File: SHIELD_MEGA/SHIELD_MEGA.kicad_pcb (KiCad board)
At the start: 2 copper layers, 101.6 x 53.3 mm, 81 parts, among them J1 Conn_02x03_Odd_Even, J10 Conn_01x03_Female, J11 DF13-6P-1.25DSA, J12 Conn_01x04_Male, J13 Conn_01x04_Male, J14 Conn_02x03_Odd_Even, J15 Conn_01x04_Male, J16 Conn_01x03_Male, J17 Conn_01x03_Male, J18 Conn_01x03_Male, J19 Conn_01x03_Male, J2 Conn_02x03_Odd_Even, J20 Conn_01x03_Male, J21 Conn_01x03_Male, J22 Conn_01x03_Male, J23 Conn_01x03_Male, J24 Conn_01x03_Male, J25 Conn_01x03_Male, J26 Conn_01x03_Male, J27 Conn_01x03_Male, J28 Conn_01x03_Male, J29 Conn_01x03_Male, J3 Conn_02x03_Odd_Even, J30 Conn_01x03_Male, J31 Conn_01x03_Male, J32 Conn_01x03_Male, J33 Conn_01x03_Male, J34 Conn_01x03_Male, J35 Conn_01x03_Male, J36 Conn_01x03_Male, J37 Conn_01x03_Male, J38 Conn_01x03_Male, J39 Conn_01x03_Male, J40 Conn_01x03_Male, J41 Conn_01x03_Male, J42 Conn_01x03_Male, J43 Conn_01x03_Male, J44 Conn_01x03_Male, J45 Conn_01x03_Male, J46 Conn_01x03_Male, J47 Conn_01x03_Male, J48 Conn_01x03_Male, J49 Conn_01x03_Male, J5 Conn_01x02_Male, J50 Conn_01x03_Male, J51 Conn_01x03_Male, J52 Conn_01x03_Male, J53 Conn_01x03_Male, J54 Conn_01x03_Male, J55 Conn_01x03_Male, J56 Conn_01x03_Male, J57 Conn_01x03_Male, J58 Conn_01x03_Male, J59 Conn_01x03_Male, J6 Conn_01x07_Female, J60 Conn_01x03_Male, J61 Conn_01x03_Male, J62 Conn_01x03_Male, J63 Conn_01x03_Male, J64 Conn_01x03_Male, J65 Conn_01x03_Male, J66 Conn_01x03_Female, J67 Conn_01x03_Female, J68 Conn_01x03_Female, J69 Conn_01x03_Female, J7 Conn_01x03_Female, J70 Conn_01x03_Female, J71 Conn_01x03_Female, J72 Conn_01x03_Female, J73 Conn_01x06_Female, J8 Conn_01x03_Female, J9 Conn_01x03_Female, SW1 SW_MEC_5E

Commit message: Changes in PCB
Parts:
- removed J14: Conn_02x03_Odd_Even, Connector_PinSocket_2.54mm:PinSocket_2x03_P2.54mm_Vertical
- removed J59, J60, J61: Conn_01x03_Male, Connector_PinHeader_2.54mm:PinHeader_1x03_P2.54mm_Vertical
- removed L1, L2: Inductor_15uH_1.9A, Inductor_SMD:L_0805_2012Metric_Pad1.15x1.40mm_HandSolder
- added D1: LED_ARBG, LED_ARBG:LED_LL-R3528RGBC-008-B, F.Cu at (135.4, 97.9)
- added G***: LOGO, LOGO:LOGO_NOVO, F.Cu at (106.3, 78.0)
- added R2: 3k3, Resistor_SMD:R_0805_2012Metric_Pad1.20x1.40mm_HandSolder, F.Cu at (143.6, 98.8)
- added R3: 3k3, Resistor_SMD:R_0805_2012Metric_Pad1.20x1.40mm_HandSolder, F.Cu at (143.7, 96.3)
- added R4: 3k3, Resistor_SMD:R_0805_2012Metric_Pad1.20x1.40mm_HandSolder, F.Cu at (143.6, 93.9)
- moved J58 127.0 mm to (129.7, 85.1)
- moved J57 120.2 mm to (132.2, 85.1)
- moved J43 107.3 mm to (188.7, 93.5), turned to 270 degrees
- moved J51 101.5 mm to (147.4, 85.1)
- moved J48 90.3 mm to (155.1, 85.1)
- moved J34 86.2 mm to (188.7, 70.6), turned to 270 degrees
- moved J45 85.8 mm to (188.7, 98.6), turned to 270 degrees
- moved J42 85.5 mm to (188.7, 90.9), turned to 270 degrees
- moved J47 83.8 mm to (157.6, 85.1)
- moved J46 77.5 mm to (160.1, 85.1)
- moved J56 73.9 mm to (134.7, 85.1)
- moved J52 61.7 mm to (144.9, 85.1)
- moved J35 57.0 mm to (188.7, 73.2), turned to 270 degrees
- moved J44 56.9 mm to (188.7, 96.0), turned to 270 degrees
- moved J53 56.6 mm to (142.4, 85.1)
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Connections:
- J12 pad 4: /arduino_mega_2560/DGND -> GND
- J13 pad 4: /arduino_mega_2560/DGND -> GND
- J15 pad 4: /arduino_mega_2560/DGND -> GND
- J16 pad 3: /arduino_mega_2560/AGND -> GND
- J17 pad 3: /arduino_mega_2560/AGND -> GND
- J18 pad 3: /arduino_mega_2560/AGND -> GND
- J19 pad 3: /arduino_mega_2560/AGND -> GND
- J20 pad 3: /arduino_mega_2560/AGND -> GND
- J21 pad 3: /arduino_mega_2560/AGND -> GND
- J22 pad 3: /arduino_mega_2560/AGND -> GND
- J23 pad 3: /arduino_mega_2560/AGND -> GND
- J24 pad 3: /arduino_mega_2560/AGND -> GND
- J25 pad 3: /arduino_mega_2560/AGND -> GND
- J26 pad 3: /arduino_mega_2560/AGND -> GND
- J27 pad 3: /arduino_mega_2560/AGND -> GND
- J28 pad 3: /arduino_mega_2560/AGND -> GND
- J29 pad 3: /arduino_mega_2560/AGND -> GND
- J3 pad 5: /arduino_mega_2560/DGND -> GND
- J30 pad 3: /arduino_mega_2560/AGND -> GND
- J31 pad 3: /arduino_mega_2560/AGND -> GND
- J32 pad 3: /arduino_mega_2560/DGND -> GND
- J33 pad 3: /arduino_mega_2560/DGND -> GND
- J34 pad 3: /arduino_mega_2560/DGND -> GND
- J35 pad 3: /arduino_mega_2560/DGND -> GND
- J36 pad 3: /arduino_mega_2560/DGND -> GND
- J37 pad 3: /arduino_mega_2560/DGND -> GND
- J38 pad 3: /arduino_mega_2560/DGND -> GND
- J39 pad 3: /arduino_mega_2560/DGND -> GND
- J40 pad 3: /arduino_mega_2560/DGND -> GND
- J41 pad 3: /arduino_mega_2560/DGND -> GND
- J42 pad 3: /arduino_mega_2560/DGND -> GND
- J43 pad 3: /arduino_mega_2560/DGND -> GND
- J44 pad 3: /arduino_mega_2560/DGND -> GND
- J45 pad 3: /arduino_mega_2560/DGND -> GND
- J46 pad 3: /arduino_mega_2560/DGND -> GND
- J47 pad 3: /arduino_mega_2560/DGND -> GND
- J48 pad 3: /arduino_mega_2560/DGND -> GND
- J49 pad 3: /arduino_mega_2560/DGND -> GND
- J50 pad 3: /arduino_mega_2560/DGND -> GND
- J51 pad 3: /arduino_mega_2560/DGND -> GND
- J52 pad 3: /arduino_mega_2560/DGND -> GND
- J53 pad 3: /arduino_mega_2560/DGND -> GND
- J54 pad 3: /arduino_mega_2560/DGND -> GND
- J55 pad 3: /arduino_mega_2560/DGND -> GND
- J56 pad 3: /arduino_mega_2560/DGND -> GND
- J57 pad 3: /arduino_mega_2560/DGND -> GND
- J58 pad 3: /arduino_mega_2560/DGND -> GND
- J62 pad 3: /arduino_mega_2560/DGND -> GND
- J63 pad 3: /arduino_mega_2560/DGND -> GND
- J64 pad 3: /arduino_mega_2560/DGND -> GND
- J65 pad 3: /arduino_mega_2560/DGND -> GND
- XA1 pad D47: /arduino_mega_2560/DIGITAL_PINS/D47 -> /B_LED
- XA1 pad D48: /arduino_mega_2560/DIGITAL_PINS/D48 -> /G_LED
- XA1 pad D49: /arduino_mega_2560/DIGITAL_PINS/D49 -> /R_LED
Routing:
- net +5V: track 0.00 -> 353.5 mm, vias 0 -> 1
- net +3V3: track 0.00 -> 198.6 mm, vias 0 -> 4
- net /arduino_mega_2560/DIGITAL_PINS/D45: track 0.00 -> 75.9 mm
- net /arduino_mega_2560/DIGITAL_PINS/D38: track 0.00 -> 74.8 mm
- net /arduino_mega_2560/DIGITAL_PINS/D43: track 0.00 -> 74.7 mm
- net /arduino_mega_2560/DIGITAL_PINS/D46: track 0.00 -> 74.1 mm
- net /arduino_mega_2560/DIGITAL_PINS/D44: track 0.00 -> 72.0 mm
- net /arduino_mega_2560/DIGITAL_PINS/D41: track 0.00 -> 71.1 mm
- net /arduino_mega_2560/DIGITAL_PINS/D39: track 0.00 -> 69.8 mm
- net /arduino_mega_2560/DIGITAL_PINS/D42: track 0.00 -> 69.8 mm
- net /arduino_mega_2560/DIGITAL_PINS/D40: track 0.00 -> 67.4 mm
- net /arduino_mega_2560/DIGITAL_PINS/D37: track 0.00 -> 63.6 mm
- net /arduino_mega_2560/DIGITAL_PINS/D36: track 0.00 -> 57.0 mm
- net /B_LED: track 0.00 -> 55.5 mm
- net /arduino_mega_2560/DIGITAL_PINS/D33: track 0.00 -> 55.4 mm
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- added copper zone on B.Cu, net GND
- added copper zone on F.Cu, net GND
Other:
- board size 101.6 x 53.3 mm -> 99.8 x 53.3 mm
- net class GND added: clearance 0.2, trace_width 0.508, via_dia 0.889, via_drill 0.4
- net class GPS added: clearance 0.16, trace_width 0.22, via_dia 0.8, via_drill 0.4
- net class desconectado added: clearance 0.16, trace_width 0.25, via_dia 0.8, via_drill 0.4
- board text added: "3V3"
- board text added: "5V"
- board text added: "A0"
- board text added: "A1"
- board text added: "A10"
- board text added: "A11"
- board text added: "A12"
- board text added: "A13"
- board text added: "A14"
- board text added: "A15"
- board text added: "A2"
- board text added: "A3"
- board text added: "A4"
- board text added: "A5"
- board text added: "A6"
- board text added: "A7"
- board text added: "A8"
- board text added: "A9"
- board text added: "ACELERÔMETRO"
- board text added: "BAROMETRO"
- board text added: "CONTROLADORA FREE PILOT"
- board text added: "D12"
- board text added: "D13"
- board text added: "D2"
- board text added: "D22"
- board text added: "D23"
- board text added: "D24"
- board text added: "D25"
- board text added: "D26"
- board text added: "D27"
- board text added: "D28"
- board text added: "D29"
- board text added: "D3"
- board text added: "D30"
- board text added: "D31"
- board text added: "D32"
- board text added: "D33"
- board text added: "D34"
- board text added: "D35"
- board text added: "D36"
- board text added: "D37"
- board text added: "D38"
- board text added: "D39"
- board text added: "D4"
- board text added: "D40"
- board text added: "D41"
- board text added: "D42"
- board text added: "D43"
- board text added: "D44"
- board text added: "D45"
- board text added: "D46"
- board text added: "D5"
- board text added: "D6"
- board text added: "D7"
- board text added: "D8"
- board text added: "D9"
- board text added: "GND"
- board text added: "GPS"
- board text added: "LINCOLN WALLACE"
- board text added: "MATHEUS CARLOS"
- board text added: "PROEX"
- board text added: "PROF. YOHAN DIAZ"
- board text added: "RADIO CONN."
- board text added: "RESET"
- board text added: "RX0"
- board text added: "RX2"
- board text added: "RX3"
- board text added: "S"
- board text added: "SCL"
- board text added: "SDA"
- board text added: "SIGNAL"
- board text added: "TX0"
- board text added: "TX2"
- board text added: "TX3"

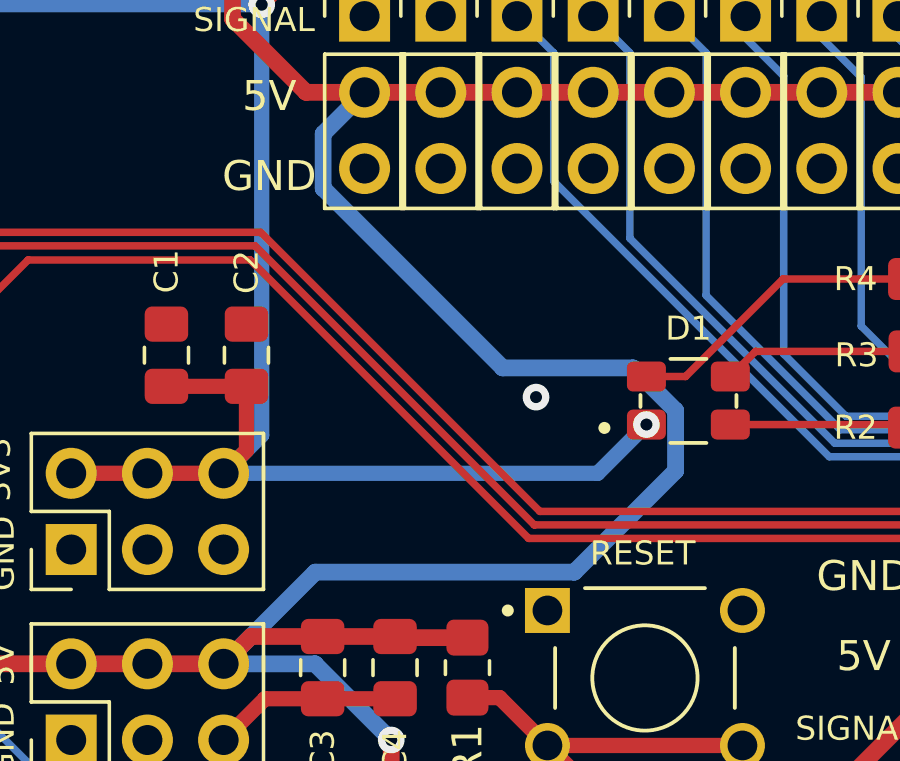
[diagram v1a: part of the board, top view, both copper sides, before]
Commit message: Roting to new alimentation of RGB LED
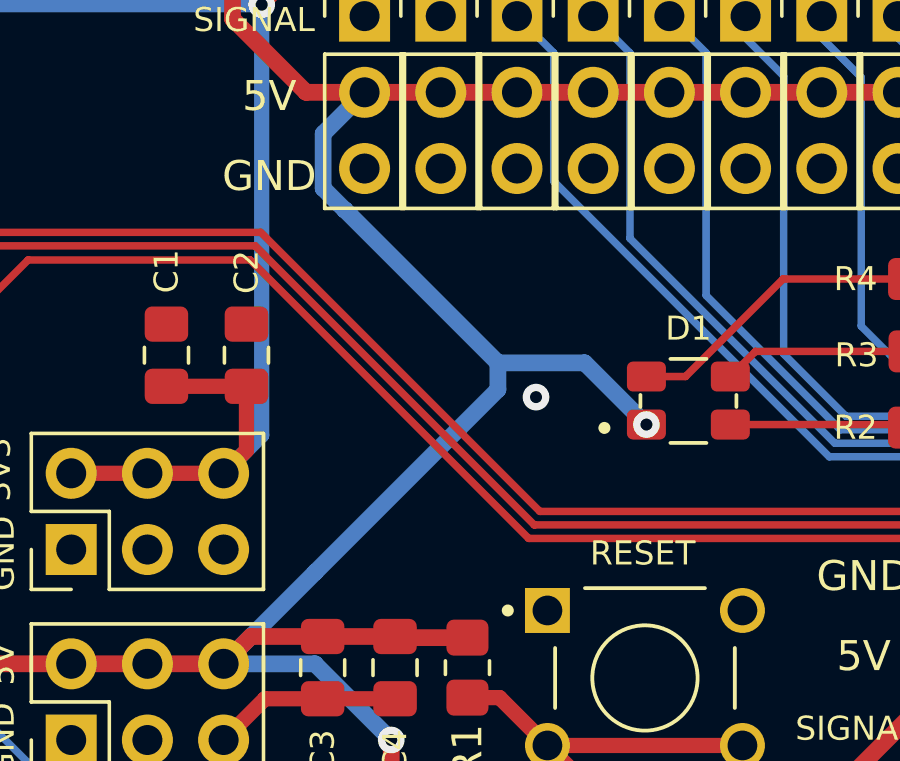
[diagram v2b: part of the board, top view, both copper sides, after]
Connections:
- D1 pad 1: +3V3 -> +5V
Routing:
- net +3V3: track 198.6 -> 183.9 mm, vias 4 -> 3
- net +5V: track 353.5 -> 346.8 mm, vias 1 -> 2

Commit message: Insert new footprint logo in bottom silkscreen
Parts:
- added G***: LOGO, LOGO:LOGO_B_SILK, B.Cu at (115.6, 79.2)
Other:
- board text added: "DEGINED BY LINCOLN WALLACE"
- board text added: "UNIFEI - 2021"
